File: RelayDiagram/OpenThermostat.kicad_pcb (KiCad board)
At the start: 2 copper layers, 162.6 x 102.4 mm, 109 parts, among them J1 Conn_01x08_Female, J2 Conn_01x15_Female, J3 Conn_01x15_Female, J4 Conn_01x09_Female, Q1 Q_NMOS_DGS, Q10 Q_NMOS_DGS, Q11 Q_NMOS_DGS, Q12 Q_NMOS_DGS, Q2 Q_NMOS_DGS, Q3 Q_NMOS_DGS, Q4 Q_NMOS_DGS, Q5 Q_NMOS_DGS, Q6 Q_NMOS_DGS, Q7 Q_NMOS_DGS, Q8 Q_NMOS_DGS, Q9 Q_NMOS_DGS, SW2 SW_Push, SW3 SW_Push, SW4 SW_Push, SW5 SW_Push, SW6 SW_Push, U1 PCF8574, U10 MB10S-13, U11 L7805CV, U2 LCD, U3 DHT11, U4 EE2-3TNU-L_DPDT_Relay, U5 EE2-3TNU-L_DPDT_Relay, U6 EE2-3TNU-L_DPDT_Relay, U7 EE2-3TNU-L_DPDT_Relay, U8 EE2-3TNU-L_DPDT_Relay, U9 EE2-3TNU-L_DPDT_Relay

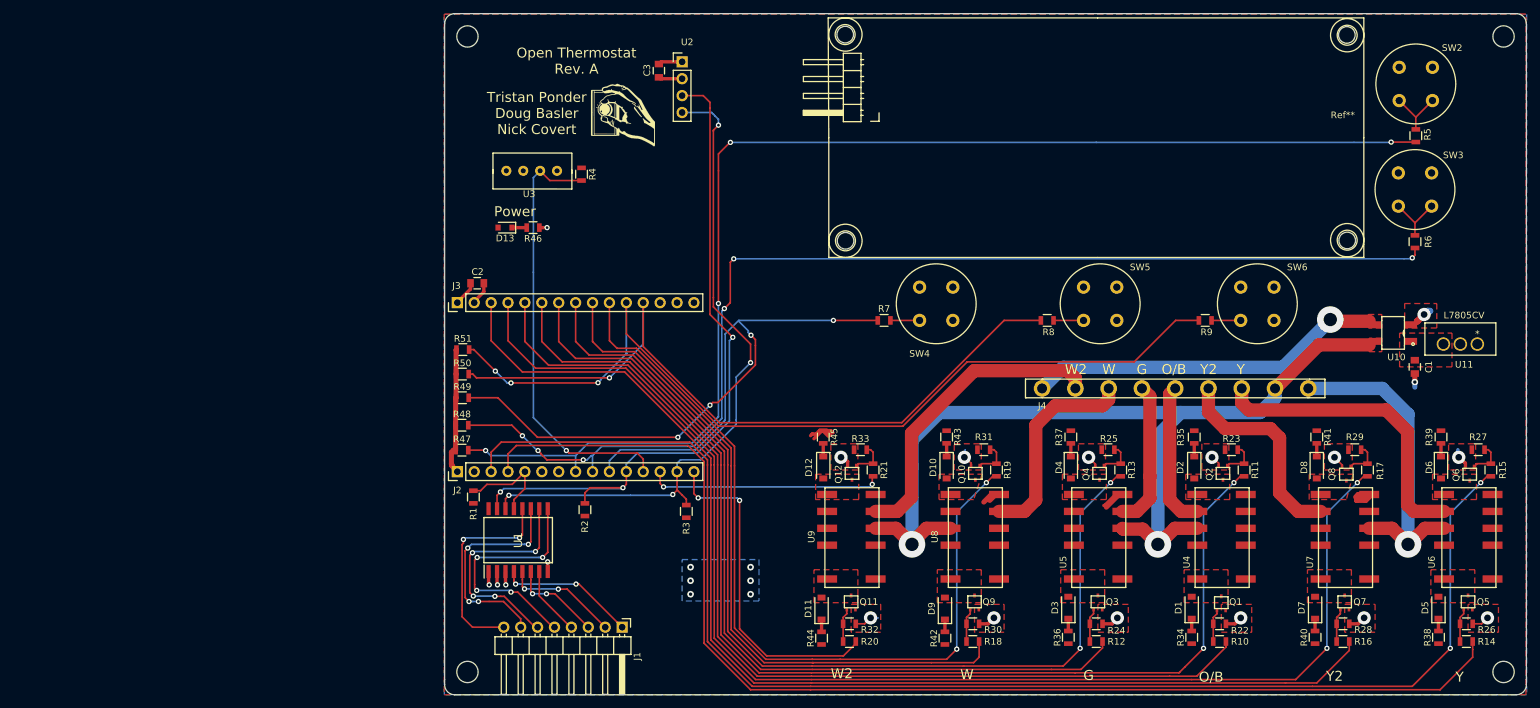
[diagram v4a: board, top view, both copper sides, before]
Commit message: Fixed relay R & RC connections, removed 1M ohm series button resistors, added 5V and GND to I/O header
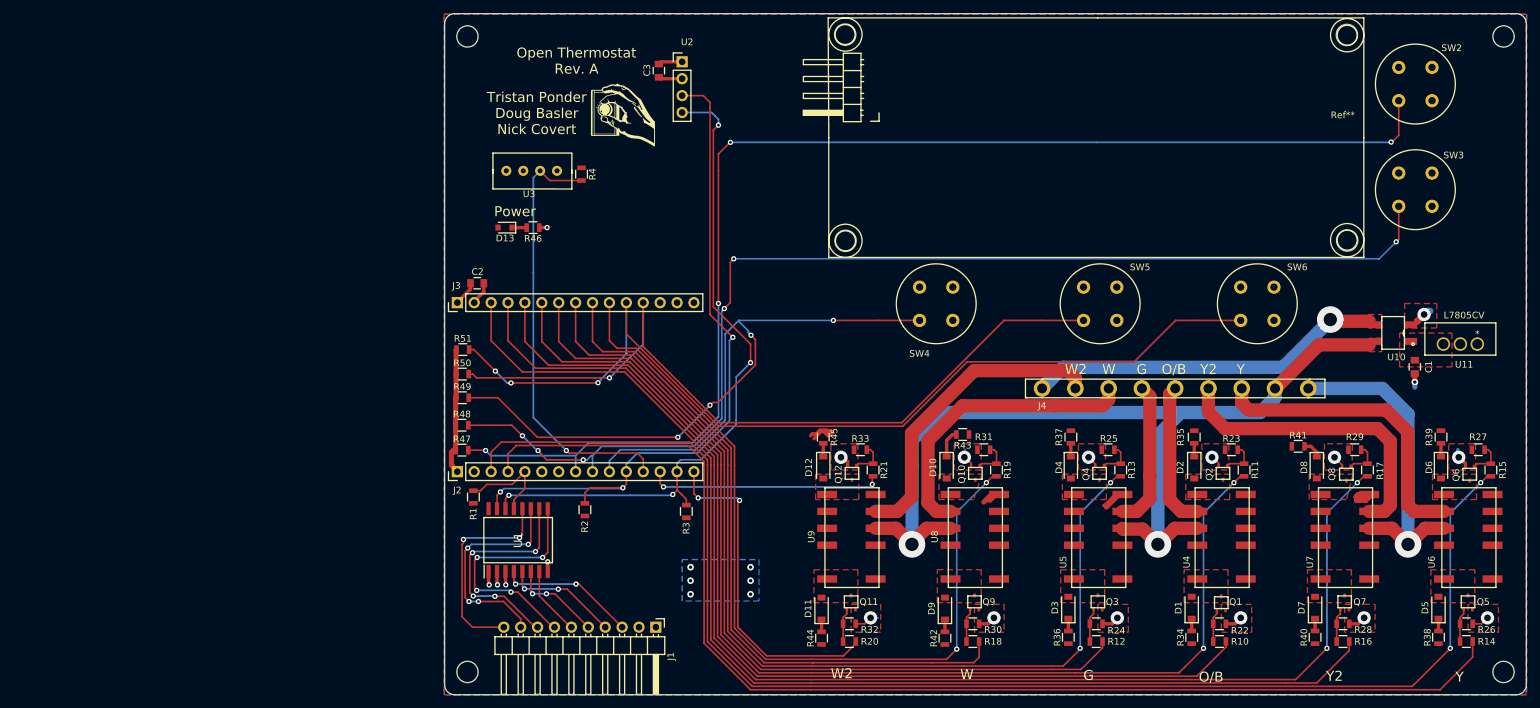
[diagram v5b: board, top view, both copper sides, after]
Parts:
- removed R5, R6, R7, R8, R9: 1M, Resistors_SMD:R_0805
- J1: value Conn_01x08_Female -> Conn_01x10_Female; footprint Pin_Headers:Pin_Header_Angled_1x08_Pitch2.54mm -> Pin_Headers:Pin_Header_Angled_1x10_Pitch2.54mm
- moved J1 5.08 mm to (82.8, 149.6)
- moved R41 3.12 mm to (179.3, 122.4), turned to 0 degrees
- moved R43 2.44 mm to (128.9, 120.7), turned to 180 degrees
- moved SW2 0.07 mm to (194.4, 70.5)
- moved SW3 0.06 mm to (194.4, 86.4)
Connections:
- J1 pad 1: Net-(J1-Pad1) -> +5V
- J1 pad 2: Net-(J1-Pad2) -> GND
- SW2 pad 1: Net-(R5-Pad2) -> Net-(J2-Pad8)
- SW3 pad 1: Net-(R6-Pad2) -> Net-(J2-Pad9)
- SW4 pad 1: Net-(R7-Pad2) -> Net-(J2-Pad10)
- SW5 pad 1: Net-(R8-Pad2) -> Net-(J3-Pad12)
- SW6 pad 1: Net-(R9-Pad2) -> Net-(J3-Pad11)
- U1 pad 10: Net-(J1-Pad6) -> Net-(J1-Pad8)
- U1 pad 11: Net-(J1-Pad7) -> Net-(J1-Pad9)
- U1 pad 12: Net-(J1-Pad8) -> Net-(J1-Pad10)
- U1 pad 4: Net-(J1-Pad1) -> Net-(J1-Pad3)
- U1 pad 5: Net-(J1-Pad2) -> Net-(J1-Pad4)
- U1 pad 6: Net-(J1-Pad3) -> Net-(J1-Pad5)
- U1 pad 7: Net-(J1-Pad4) -> Net-(J1-Pad6)
- U1 pad 9: Net-(J1-Pad5) -> Net-(J1-Pad7)
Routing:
- net Net-(J1-Pad9): track 0.00 -> 33.4 mm, vias 0 -> 4
- net Net-(J1-Pad10): track 0.00 -> 31.7 mm, vias 0 -> 2
- net Net-(J1-Pad6): track 34.7 -> 10.6 mm, vias 4 -> 0
- net Net-(J1-Pad5): track 36.7 -> 14.2 mm, vias 4 -> 2
- net Net-(J1-Pad1): track 20.7 -> 0.00 mm, vias 2 -> 0
- net Net-(J1-Pad2): track 17.2 -> 0.00 mm, vias 2 -> 0
- net Net-(J4-Pad6): track 31.4 -> 45.9 mm
- net Net-(J4-Pad3): track 31.7 -> 44.7 mm
- net Net-(R6-Pad2): track 8.95 -> 0.00 mm
- net Net-(R5-Pad2): track 8.90 -> 0.00 mm
- net Net-(J1-Pad4): track 10.6 -> 17.2 mm, vias 0 -> 2
- net Net-(J1-Pad3): track 14.2 -> 20.7 mm
- net Net-(J3-Pad12): track 112.2 -> 118.7 mm
- net Net-(J3-Pad11): track 138.4 -> 144.7 mm
- net Net-(J2-Pad10): track 116.1 -> 122.4 mm
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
